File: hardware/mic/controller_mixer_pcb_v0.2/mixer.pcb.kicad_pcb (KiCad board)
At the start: 4 copper layers, 184.2 x 270.5 mm, 185 parts, among them U5 Teensy4.1

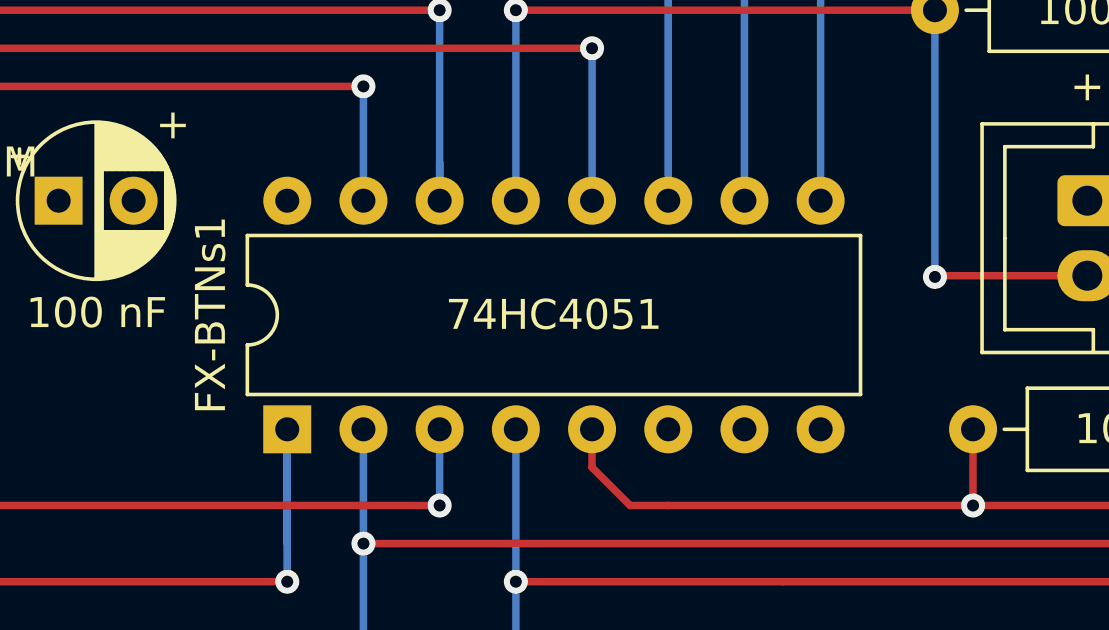
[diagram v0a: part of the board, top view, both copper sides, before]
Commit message: CC BY-NC-SA 4.0 license for hardware ready
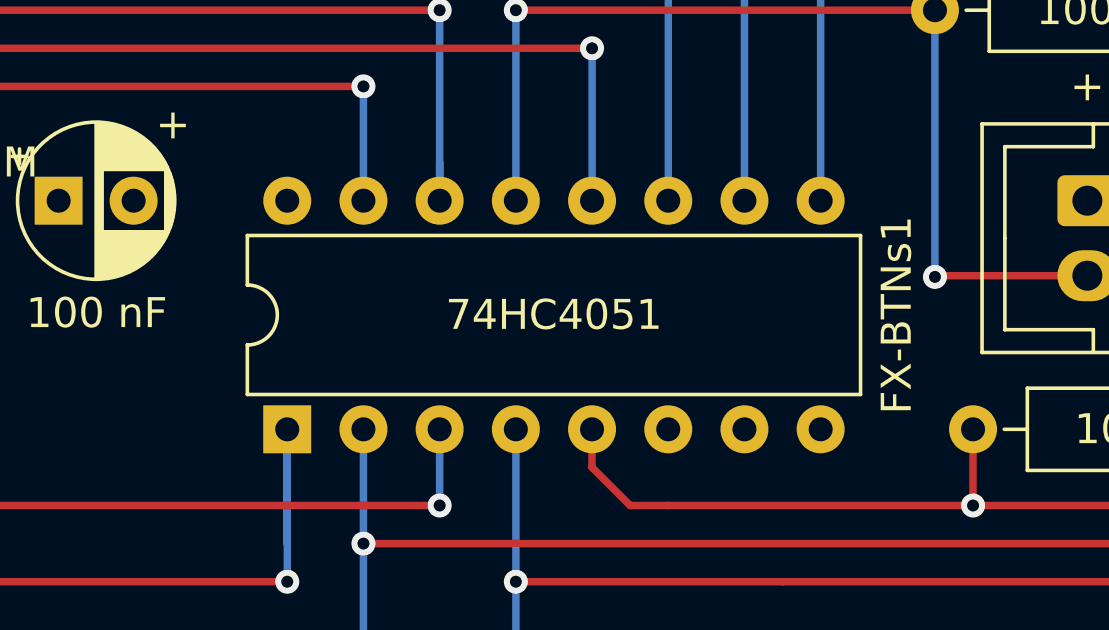
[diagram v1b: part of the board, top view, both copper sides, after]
